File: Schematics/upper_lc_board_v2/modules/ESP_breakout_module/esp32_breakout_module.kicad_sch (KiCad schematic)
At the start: 23 parts, among them J1 USB_C_Female_USB2_Small, SW1 SW_ESP_BOOT_MODE, SW2 SW_ESP_RESET, U1 ESP32-S3-WROOM-1-N16, U2 ISO1044BDR

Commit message: pcb design
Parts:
- added BZ1: Buzzer, Buzzer_Beeper:Buzzer_TDK_PS1240P02BT_D12.2mm_H6.5mm, symbol Device:Buzzer
- added C23, C27: 0.1uF, Capacitor_SMD:C_0603_1608Metric, symbol Device:C
- added D15: 1N4148WS-7-F, Diode_SMD:D_SOD-323, symbol Diode:1N4148WS
- added Q4: 2N7002, Package_TO_SOT_SMD:SOT-23, symbol Transistor_FET:2N7002
- added R27: 220, Resistor_SMD:R_0603_1608Metric, symbol Device:R
- added R28: 10K, Resistor_SMD:R_0603_1608Metric, symbol Device:R
- added R29: 1k, Resistor_SMD:R_0603_1608Metric, symbol Device:R
- added R30: 470, Resistor_SMD:R_0603_1608Metric, symbol Device:R
- J1: footprint USBC-CONN:USB_C_DB-108PWB -> Connector_USB:USB_C_Receptacle_GCT_USB4105-xx-A_16P_TopMnt_Horizontal
- U2: footprint ul_ISO1044BDR:SOIC_1044BDR_TEX -> ul_ISO1044BDR:SOIC127P600X175-8N
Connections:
- net +3V3: now also BZ1.1 (+), C23.1, D15.1 (K), R29.2
- net +5V: now also C27.1
- net GND: now also C23.2, C27.2, Q4.2 (S), R28.1
- net GPIO_01: now also U2.2 (TXD)
- net GPIO_02: now also U2.3 (RXD)
- net GPIO_35: now also R2.1
- net GPIO_36: now also R3.1
- net GPIO_37: now also R4.1
- net GPIO_38: no longer U2.2 (TXD)
- net GPIO_39: no longer U2.3 (RXD)
- net GPIO_40: no longer R4.1
- net GPIO_42: now also R30.1; no longer R2.1
- net GPIO_45: no longer D4.2 (DOUT)
- net HALL_SDA: now reaches U1.10 (IO17)
- net GPIO_46: now reaches U1.16 (IO46)
- net ADC_DRDY: now reaches U1.23 (IO21)
- net GPIO_47: now reaches U1.24 (IO47)
- net CAN_+ renamed CAN_P
- net CAN_- renamed CAN_N
- net GPIO_03 renamed VALVE1_CTRL
- net GPIO_09 renamed VALVE2_CTRL
- net GPIO_10 renamed VSOL-SW
- net GPIO_11 renamed ADC_CLKIN
- net GPIO_12 renamed SPI_MOSI
- net GPIO_13 renamed SPI_MISO
- net GPIO_14 renamed SPI_SCLK
- net GPIO_18 renamed HALL_SCL
- net GPIO_41 renamed BUZZ_IN
- net BUZZ_IN: now also R27.2; no longer R3.1
- net GPIO_48: no longer names the net of U1.25 (IO48)
- new net: Q4.1 (G), R27.1, R28.2
- new net: D4.2 (DOUT), R30.2
- new net: BZ1.2 (-), D15.2 (A), Q4.3 (D), R29.1
- no-connect marks 16 -> 13
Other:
- note added: "Signal Buzzer"
- moved on the sheet: C1, C2, C3, C4, C5, C6, C7, D1, D2, D3, D4, J1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

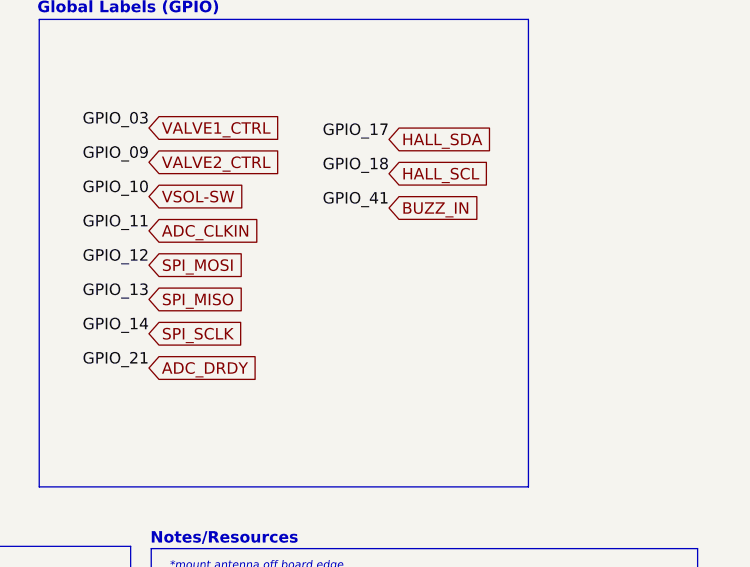
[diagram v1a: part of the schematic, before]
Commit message: add silkscreen
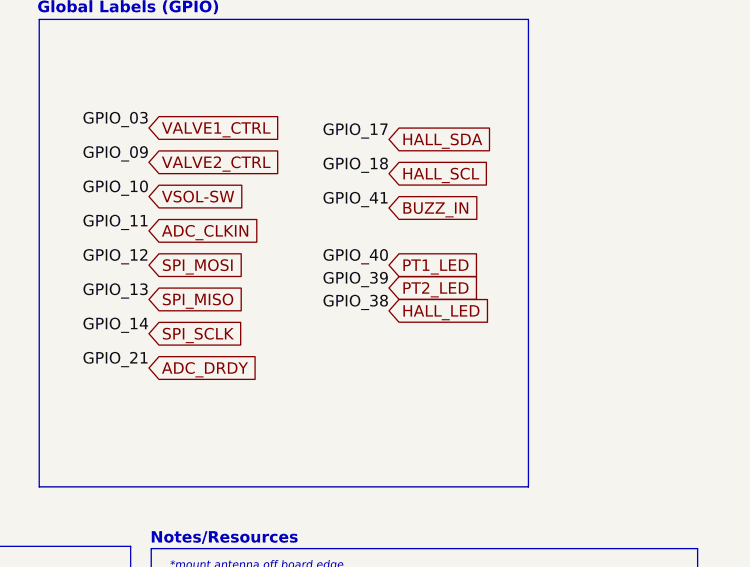
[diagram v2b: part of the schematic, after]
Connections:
- net GPIO_38 renamed HALL_LED
- net GPIO_39 renamed PT2_LED
- net GPIO_40 renamed PT1_LED
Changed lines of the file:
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@@
+		)
+	)
+	(label "GPIO_38"
+		(at 194.31 113.03 180)
+		(fields_autoplaced yes)
+		(effects
+			(font
+				(size 1.27 1.27)
+			)
+			(justify right bottom)
 		)
 	)
@@
 		)
 	)
+	(label "GPIO_39"
+		(at 194.31 110.49 180)
+		(fields_autoplaced yes)
+		(effects
+			(font
+				(size 1.27 1.27)
+			)
+			(justify right bottom)
+		)
+	)
 	(label "GPIO_42"
 		(at 73.66 100.33 0)
@@
 		)
 	)
+	(label "GPIO_40"
+		(at 194.31 107.95 180)
+		(fields_autoplaced yes)
+		(effects
+			(font
+				(size 1.27 1.27)
+			)
+			(justify right bottom)
+		)
+	)
 	(label "GPIO_09"
 		(at 167.64 96.52 180)
@@
 		)
 	)
+	(global_label "PT2_LED"
+		(shape input)
+		(at 194.31 110.49 0)
+		(fields_autoplaced yes)
+		(effects
+			(font
+				(size 1.27 1.27)
+			)
+			(justify left)
+		)
+		(property "Intersheetrefs" "${INTERSHEET_REFS}"
+			(at 205.157 110.49 0)
+			(effects
+				(font
+					(size 1.27 1.27)
+				)
+				(justify left)
+				(hide yes)
+			)
+		)
+	)
 	(global_label "VALVE1_CTRL"
 		(shape input)
@@
 		)
 	)
+	(global_label "HALL_LED"
+		(shape input)
+		(at 194.31 113.03 0)
+		(fields_autoplaced yes)
+		(effects
+			(font
+				(size 1.27 1.27)
+			)
+			(justify left)
+		)
+		(property "Intersheetrefs" "${INTERSHEET_REFS}"
+			(at 206.1852 113.03 0)
+			(effects
+				(font
+					(size 1.27 1.27)
+				)
+				(justify left)
+				(hide yes)
+			)
+		)
+	)
 	(global_label "CAN_N"
 		(shape input)
@@
 			(effects
 				(font
+					(size 1.27 1.27)
+				)
+				(justify left)
+				(hide yes)
+			)
+		)
+	)
+	(global_label "PT1_LED"
+		(shape input)
+		(at 194.31 107.95 0)
+		(fields_autoplaced yes)
+		(effects
+			(font
+				(size 1.27 1.27)
+			)
+			(justify left)
+		)
+		(property "Intersheetrefs" "${INTERSHEET_REFS}"
+			(at 205.157 107.95 0)
+			(effects
+				(font

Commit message: small adjusmetns
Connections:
- net GPIO_47 renamed VPT-SW
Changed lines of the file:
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@@
+		)
+	)
+	(label "GPIO_47"
+		(at 194.31 118.11 180)
+		(fields_autoplaced yes)
+		(effects
+			(font
+				(size 1.27 1.27)
+				(color 0 0 0 1)
+			)
+			(justify right bottom)
 		)
 	)
@@
 			(effects
 				(font
+					(size 1.27 1.27)
+				)
+				(justify left)
+				(hide yes)
+			)
+		)
+	)
+	(global_label "VPT-SW"
+		(shape input)
+		(at 194.31 118.11 0)
+		(fields_autoplaced yes)
+		(effects
+			(font
+				(size 1.27 1.27)
+			)
+			(justify left)
+		)
+		(property "Intersheetrefs" "${INTERSHEET_REFS}"
+			(at 204.8547 118.11 0)
+			(effects
+				(font

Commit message: review work
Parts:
- removed C5: 0.1uF, Capacitor_SMD:C_0603_1608Metric, symbol Device:C
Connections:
- net VSOL-SW is gone; now on net VALVE2_CTRL: U1.18 (IO10)
- net GPIO_35: now also R4.1; no longer R2.1
- net GPIO_37: now also R2.1; no longer R4.1
- net VALVE1_CTRL: now also U1.17 (IO9); no longer U1.15 (IO3)
- net VALVE2_CTRL: no longer U1.17 (IO9)
- net HALL_LED renamed GPIO_38
- net PT1_LED renamed GPIO_40
- net PT2_LED renamed GPIO_39
- new net GPIO_03: U1.15 (IO3)
